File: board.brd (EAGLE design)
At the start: 82 parts, among them J1 AVR_SPI_PRG_6NS, U2 USD-SOCKETNEW, U3 MAX1555, U4 TPS2112A, U6 74HC595, U7 3.3V, U8 2.8V, Y1 12.288MHz, Y2 8MHz

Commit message: Finished layout
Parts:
- added R26, R28: 10k, rcl:R0603W
- added R27: 10k, rcl:R0603
- moved C33 16.5 mm to (37.5, 30.5), turned to 0 degrees
- moved C18 0.32 mm to (10.5, 25.4)
- moved R17 0.32 mm to (25.1, 30.2)
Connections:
- net CHG_B: now also U$1.23
- net DS: now also U$1.12
- net ENCODER_A: now also U$1.7
- net ENCODER_B: now also U$1.5
- net ENCODER_S: now also U$1.6
- net MP3_XCS: now also R26.1
- net MP3_XDCS: now also R28.1, U$1.21; no longer U$1.23
- net SD_CS: now also R27.1
- net SHCP: now also U$1.10
- net STCP: now also U$1.11
- net VDD: now also R26.2, R27.2, R28.2
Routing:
- net VDD: track 88.9 -> 250.1 mm, vias 5 -> 8
- net SD_CS: track 0.00 -> 46.8 mm, vias 0 -> 2
- net ENCODER_B: track 0.00 -> 42.8 mm, vias 0 -> 2
- net ENCODER_S: track 0.00 -> 41.8 mm, vias 0 -> 2
- net ENCODER_A: track 0.00 -> 40.5 mm, vias 0 -> 2
- net MISO: track 58.4 -> 88.6 mm, vias 2 -> 3
- net SCK: track 52.7 -> 78.9 mm
- net MOSI: track 65.9 -> 91.9 mm
- net CHG_B: track 12.3 -> 27.2 mm, vias 1 -> 2
- net GND: track 51.8 -> 58.4 mm, vias 7 -> 13
- net MP3_XCS: track 23.5 -> 29.1 mm
- net DS: track 14.8 -> 19.3 mm
- net STCP: track 12.9 -> 16.2 mm
- net SHCP: track 12.0 -> 14.9 mm
- net CVDD: track 71.1 -> 73.6 mm
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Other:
- board text added: "2.0"
- board text added: "MJK 09/13 mattkeeter.com"
- board text removed: "1.0"
- board text removed: "MJK 06/13 mattkeeter.com"
- board text removed: "OFF"

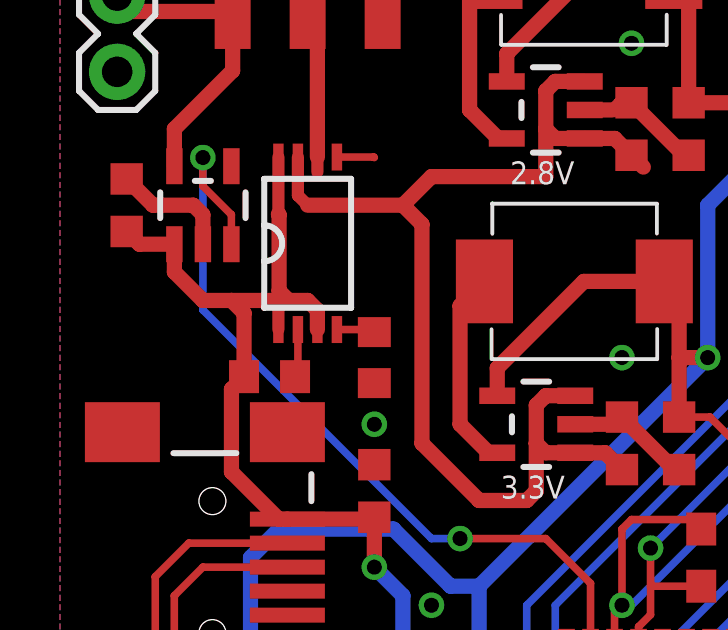
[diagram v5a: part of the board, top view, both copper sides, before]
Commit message: Not sure why I shorted VDD with an open-drain output to ground.
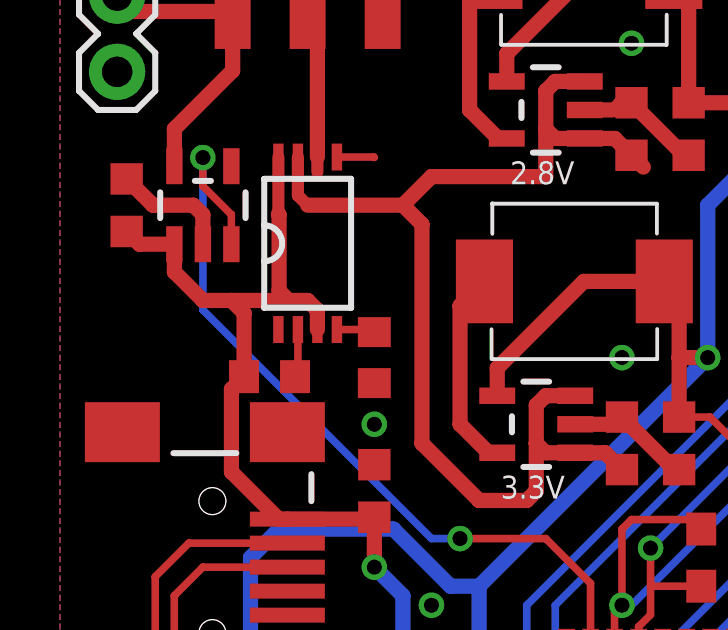
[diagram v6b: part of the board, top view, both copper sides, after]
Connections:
- net VBUS: no longer U4.1
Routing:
- net VBUS: track 40.9 -> 39.9 mm
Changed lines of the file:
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@@
 <contactref element="U4" pad="3"/>
 <contactref element="R13" pad="2"/>
-<contactref element="U4" pad="1"/>
 <contactref element="U4" pad="8"/>
-<wire x1="7.28" y1="30.78" x2="7.28" y2="31.75" width="0.4064" layer="1"/>
 <wire x1="8.58" y1="30.78" x2="8.58" y2="31.425" width="0.508" layer="1"/>
 <wire x1="8.58" y1="31.425" x2="8.255" y2="31.75" width="0.508" layer="1"/>

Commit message: Switched to 0603W packages for audio path resistors
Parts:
- R2, R3, R5, R6, R7, R8: device rcl:R0603 -> rcl:R0603W

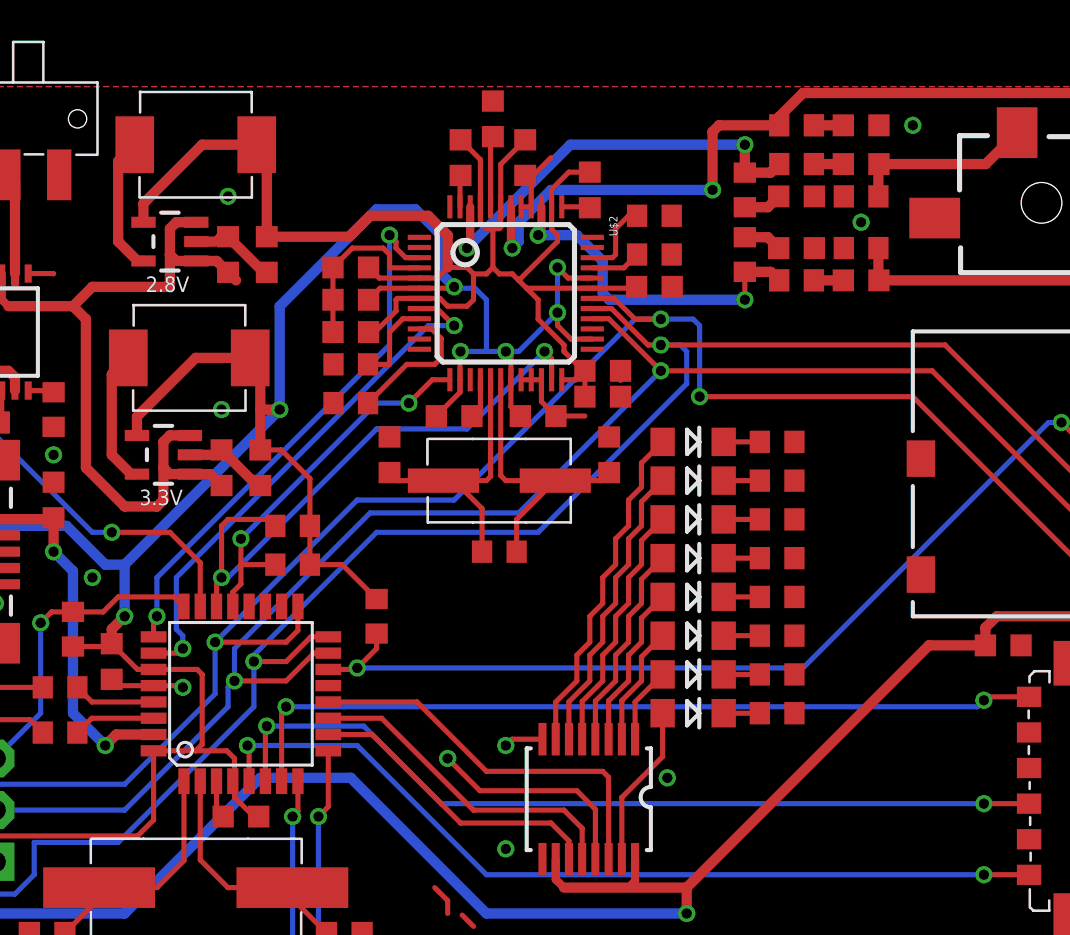
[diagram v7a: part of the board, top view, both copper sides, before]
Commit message: Shifted VS1003 over a bit
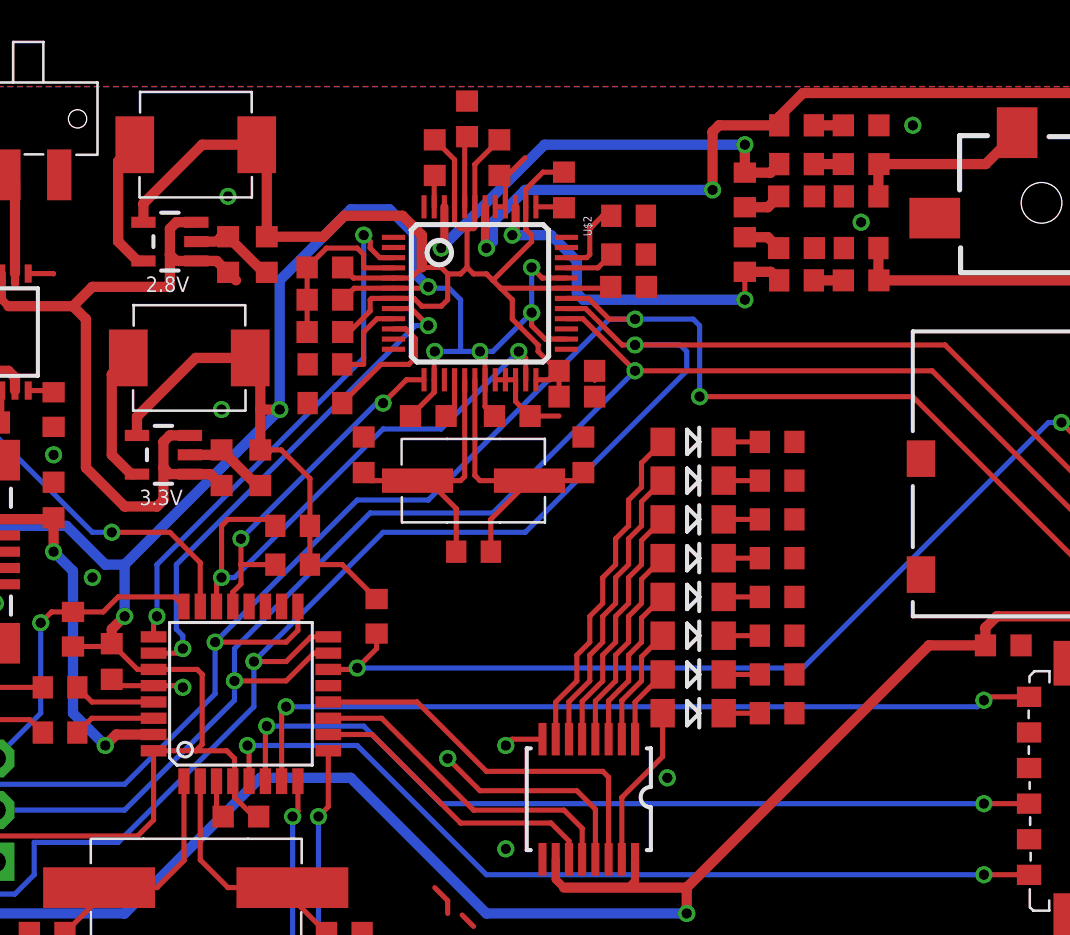
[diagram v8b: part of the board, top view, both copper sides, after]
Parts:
- moved C1 1.27 mm to (30.8, 44.1)
- moved C10 1.27 mm to (36.2, 31.8)
- moved C3 1.27 mm to (28.9, 29.5)
- moved C33 1.27 mm to (36.2, 30.5)
- moved C5 1.27 mm to (32.4, 42.2)
- moved C8 1.27 mm to (38.7, 35.9)
- moved R14 1.27 mm to (38.7, 37.5)
- moved R15 1.27 mm to (38.7, 39.4)
- moved C11 1.27 mm to (29.2, 42.2)
- moved C19 1.27 mm to (25.7, 27.6)
- moved C4 1.27 mm to (23.8, 35.2)
- moved C6 1.27 mm to (23.8, 33.7)
- moved C9 1.27 mm to (23.8, 36.8)
- moved R1 1.27 mm to (31.1, 22.9)
- moved R16 1.27 mm to (23.8, 32.1)
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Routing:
- net MOSI: track 91.9 -> 94.2 mm
- net MP3_XCS: track 29.1 -> 27.8 mm
- net GBUF: track 42.5 -> 43.8 mm
- net MP3_XDCS: track 18.7 -> 17.4 mm
- net LEFT: track 21.1 -> 22.4 mm
- net CVDD: track 73.6 -> 72.3 mm
- net RIGHT: track 17.1 -> 18.4 mm
- net MP3_DREQ: track 26.0 -> 25.1 mm
- net MP3_XRESET: track 26.7 -> 26.1 mm
- net VDD: track 250.1 -> 249.6 mm
